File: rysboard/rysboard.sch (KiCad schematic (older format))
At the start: 9 parts, among them J1 RPi4, J17 Conn_01x03, J18 Conn_01x05, U4 STM32G031K8Ux

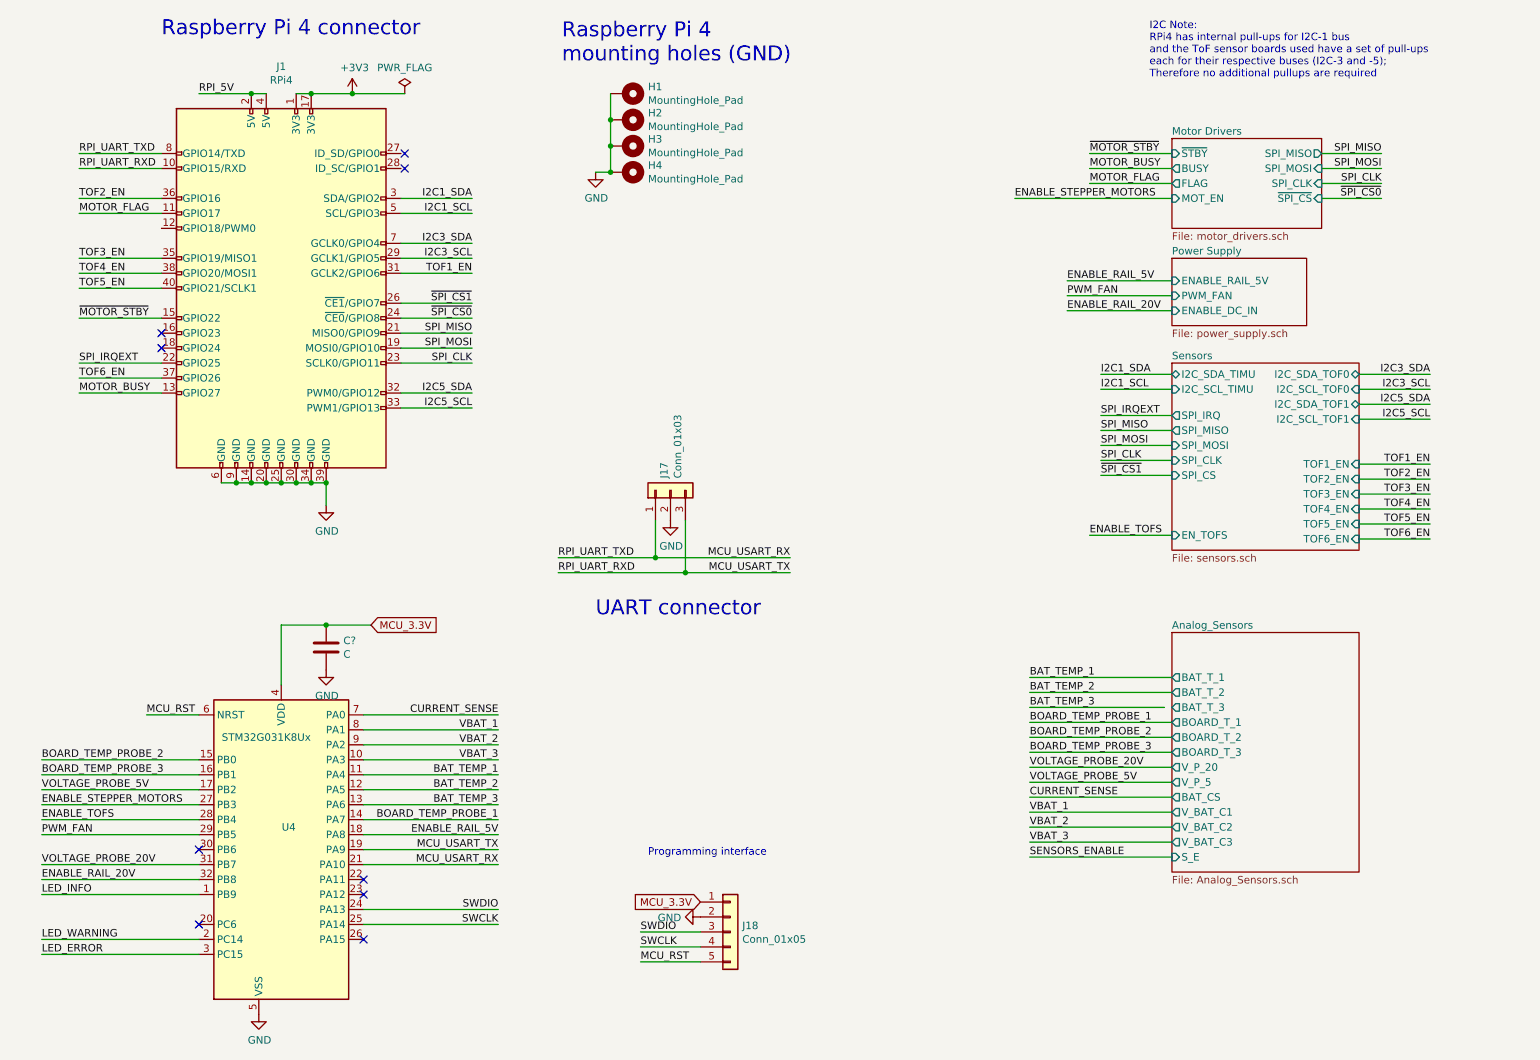
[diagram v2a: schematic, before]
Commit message: new mosfet footprints
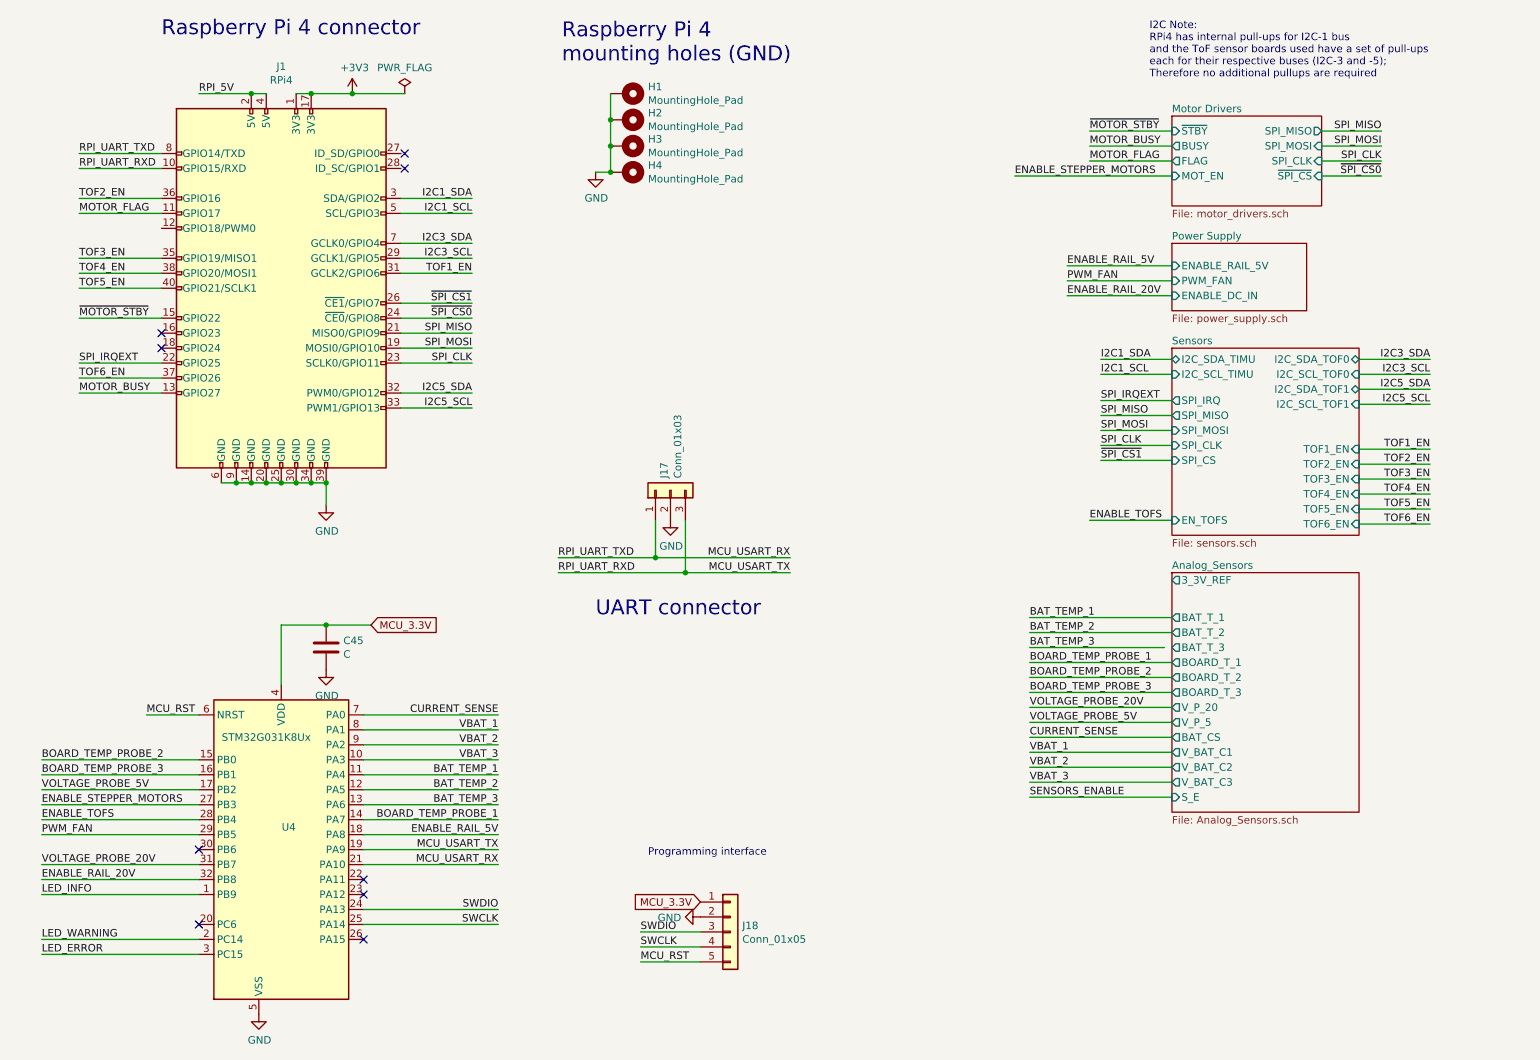
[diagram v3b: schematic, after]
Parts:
- gave numbers to parts that had none: 1
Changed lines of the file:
@@
 Raspberry Pi 4 connector
 $Sheet
-S 8250 2300 900  450
+S 8250 2200 900  450
 U 5E8FCBC6
 F0 "Power Supply" 50
 F1 "power_supply.sch" 50
-F2 "ENABLE_RAIL_5V" I L 8250 2450 50
-F3 "PWM_FAN" I L 8250 2550 50
-F4 "ENABLE_DC_IN" I L 8250 2650 50
+F2 "ENABLE_RAIL_5V" I L 8250 2350 50
+F3 "PWM_FAN" I L 8250 2450 50
+F4 "ENABLE_DC_IN" I L 8250 2550 50
 $EndSheet
 Text Label 3575 2700 2    50   ~ 0
@@
 Text Label 950  3200 0    50   ~ 0
 MOTOR_BUSY
-Text Label 7700 1800 0    50   ~ 0
+Text Label 7700 1650 0    50   ~ 0
 MOTOR_FLAG
-Text Label 7700 1600 0    50   ~ 0
+Text Label 7700 1450 0    50   ~ 0
 ~MOTOR_STBY
-Text Label 7700 1700 0    50   ~ 0
+Text Label 7700 1550 0    50   ~ 0
 MOTOR_BUSY
-Text Label 9650 1600 2    50   ~ 0
+Text Label 9650 1450 2    50   ~ 0
 SPI_MISO
-Text Label 9650 1700 2    50   ~ 0
+Text Label 9650 1550 2    50   ~ 0
 SPI_MOSI
-Text Label 9650 1800 2    50   ~ 0
+Text Label 9650 1650 2    50   ~ 0
 SPI_CLK
-Text Label 9650 1900 2    50   ~ 0
+Text Label 9650 1750 2    50   ~ 0
 ~SPI_CS0
+Text Label 7775 3350 0    50   ~ 0
+SPI_MISO
 Text Label 7775 3450 0    50   ~ 0
-SPI_MISO
+SPI_MOSI
 Text Label 7775 3550 0    50   ~ 0
-SPI_MOSI
+SPI_CLK
 Text Label 7775 3650 0    50   ~ 0
-SPI_CLK
-Text Label 7775 3750 0    50   ~ 0
 ~SPI_CS1
 Wire Wire Line
-	8250 3450 7775 3450
-Wire Wire Line
-	7775 3550 8250 3550
-Wire Wire Line
-	8250 3650 7775 3650
-Wire Wire Line
-	7775 3750 8250 3750
+	8250 3350 7775 3350
+Wire Wire Line
+	7775 3450 8250 3450
+Wire Wire Line
+	8250 3550 7775 3550
+Wire Wire Line
+	7775 3650 8250 3650
+Wire Wire Line
+	9500 3575 9975 3575
 Wire Wire Line
 	9500 3675 9975 3675
+Text Label 9975 3575 2    50   ~ 0
+TOF1_EN
+Text Label 9975 3675 2    50   ~ 0
+TOF2_EN
+Text Label 7775 3250 0    50   ~ 0
+SPI_IRQEXT
 Wire Wire Line
 	9500 3775 9975 3775
-Text Label 9975 3675 2    50   ~ 0
-TOF1_EN
 Text Label 9975 3775 2    50   ~ 0
-TOF2_EN
-Text Label 7775 3350 0    50   ~ 0
-SPI_IRQEXT
+TOF3_EN
+Text Label 9975 3875 2    50   ~ 0
+TOF4_EN
+Text Label 9975 3975 2    50   ~ 0
+TOF5_EN
+Text Label 9975 4075 2    50   ~ 0
+TOF6_EN
 Wire Wire Line
 	9500 3875 9975 3875
-Text Label 9975 3875 2    50   ~ 0
-TOF3_EN
-Text Label 9975 3975 2    50   ~ 0
-TOF4_EN
-Text Label 9975 4075 2    50   ~ 0
-TOF5_EN
-Text Label 9975 4175 2    50   ~ 0
-TOF6_EN
 Wire Wire Line
 	9500 3975 9975 3975
 Wire Wire Line
 	9500 4075 9975 4075
-Wire Wire Line
-	9500 4175 9975 4175
 NoConn ~ 3125 1700
 NoConn ~ 3125 1600
@@
 I2C5_SCL
 Wire Wire Line
-	7775 3350 8250 3350
+	7775 3250 8250 3250
 $Sheet
-S 8250 3000 1250 1250
+S 8250 2900 1250 1250
 U 5EA6D11C
 F0 "Sensors" 50
 F1 "sensors.sch" 50
-F2 "TOF6_EN" I R 9500 4175 50
-F3 "TOF5_EN" I R 9500 4075 50
-F4 "TOF4_EN" I R 9500 3975 50
-F5 "TOF2_EN" I R 9500 3775 50
-F6 "TOF1_EN" I R 9500 3675 50
-F7 "TOF3_EN" I R 9500 3875 50
-F8 "SPI_MOSI" I L 8250 3550 50
-F9 "SPI_MISO" O L 8250 3450 50
-F10 "SPI_CLK" I L 8250 3650 50
-F11 "SPI_CS" I L 8250 3750 50
-F12 "SPI_IRQ" O L 8250 3350 50
-F13 "I2C_SCL_TOF0" I R 9500 3175 50
-F14 "I2C_SDA_TOF0" B R 9500 3075 50
-F15 "I2C_SCL_TIMU" I L 8250 3175 50
-F16 "I2C_SDA_TIMU" B L 8250 3075 50
-F17 "I2C_SCL_TOF1" I R 9500 3375 50
-F18 "I2C_SDA_TOF1" B R 9500 3275 50
-F19 "EN_TOFS" I L 8250 4150 50
+F2 "TOF6_EN" I R 9500 4075 50
+F3 "TOF5_EN" I R 9500 3975 50
+F4 "TOF4_EN" I R 9500 3875 50
+F5 "TOF2_EN" I R 9500 3675 50
+F6 "TOF1_EN" I R 9500 3575 50
+F7 "TOF3_EN" I R 9500 3775 50
+F8 "SPI_MOSI" I L 8250 3450 50
+F9 "SPI_MISO" O L 8250 3350 50
+F10 "SPI_CLK" I L 8250 3550 50
+F11 "SPI_CS" I L 8250 3650 50
+F12 "SPI_IRQ" O L 8250 3250 50
+F13 "I2C_SCL_TOF0" I R 9500 3075 50
+F14 "I2C_SDA_TOF0" B R 9500 2975 50
+F15 "I2C_SCL_TIMU" I L 8250 3075 50
+F16 "I2C_SDA_TIMU" B L 8250 2975 50
+F17 "I2C_SCL_TOF1" I R 9500 3275 50
+F18 "I2C_SDA_TOF1" B R 9500 3175 50
+F19 "EN_TOFS" I L 8250 4050 50
 $EndSheet
 $Comp
@@
 RPI_UART_RXD
 Wire Wire Line
+	9500 2975 9975 2975
+Wire Wire Line
 	9500 3075 9975 3075
 Wire Wire Line
+	9500 3275 9975 3275
+Wire Wire Line
 	9500 3175 9975 3175
 Wire Wire Line
-	9500 3375 9975 3375
-Wire Wire Line
-	9500 3275 9975 3275
+	7775 2975 8250 2975
 Wire Wire Line
 	7775 3075 8250 3075
-Wire Wire Line
-	7775 3175 8250 3175
+Text Label 7775 2975 0    50   ~ 0
+I2C1_SDA
 Text Label 7775 3075 0    50   ~ 0
-I2C1_SDA
-Text Label 7775 3175 0    50   ~ 0
 I2C1_SCL
+Text Label 9975 2975 2    50   ~ 0
+I2C3_SDA
 Text Label 9975 3075 2    50   ~ 0
-I2C3_SDA
+I2C3_SCL
 Text Label 9975 3175 2    50   ~ 0
-I2C3_SCL
+I2C5_SDA
 Text Label 9975 3275 2    50   ~ 0
-I2C5_SDA
-Text Label 9975 3375 2    50   ~ 0
 I2C5_SCL
 Text Label 3575 2400 2    50   ~ 0
@@
 	4150 4400 5000 4400
 Connection ~ 5000 4400
+Text Label 7550 2350 0    50   ~ 0
+ENABLE_RAIL_5V
 Text Label 7550 2450 0    50   ~ 0
-ENABLE_RAIL_5V
+PWM_FAN
 Text Label 7550 2550 0    50   ~ 0
-PWM_FAN
-Text Label 7550 2650 0    50   ~ 0
 ENABLE_RAIL_20V
 Wire Wire Line
+	7550 2350 8250 2350
+Wire Wire Line
 	7550 2450 8250 2450
 Wire Wire Line
 	7550 2550 8250 2550
-Wire Wire Line
-	7550 2650 8250 2650
-Text Label 7700 4150 0    50   ~ 0
+Text Label 7700 4050 0    50   ~ 0
 ENABLE_TOFS
 Wire Wire Line
-	7700 4150 8250 4150
+	7700 4050 8250 4050
 $Sheet
-S 8250 4800 1250 1600
+S 8250 4400 1250 1600
 U 60370950
 F0 "Analog_Sensors" 50
 F1 "Analog_Sensors.sch" 50
-F2 "BAT_T_1" O L 8250 5100 50
-F3 "BAT_T_2" O L 8250 5200 50
-F4 "BAT_T_3" O L 8250 5300 50
-F5 "BOARD_T_1" O L 8250 5400 50
-F6 "BOARD_T_2" O L 8250 5500 50
-F7 "BOARD_T_3" O L 8250 5600 50
-F8 "V_P_20" O L 8250 5700 50
-F9 "V_P_5" O L 8250 5800 50
-F10 "BAT_CS" O L 8250 5900 50
-F11 "V_BAT_C1" O L 8250 6000 50
-F12 "V_BAT_C2" O L 8250 6100 50
-F13 "V_BAT_C3" O L 8250 6200 50
-F14 "S_E" I L 8250 6300 50
+F2 "BAT_T_1" O L 8250 4700 50
+F3 "BAT_T_2" O L 8250 4800 50
+F4 "BAT_T_3" O L 8250 4900 50
+F5 "BOARD_T_1" O L 8250 5000 50
+F6 "BOARD_T_2" O L 8250 5100 50
+F7 "BOARD_T_3" O L 8250 5200 50
+F8 "V_P_20" O L 8250 5300 50
+F9 "V_P_5" O L 8250 5400 50
+F10 "BAT_CS" O L 8250 5500 50
+F11 "V_BAT_C1" O L 8250 5600 50
+F12 "V_BAT_C2" O L 8250 5700 50
+F13 "V_BAT_C3" O L 8250 5800 50
+F14 "S_E" I L 8250 5900 50
+F15 "3_3V_REF" O L 8250 4450 50
 $EndSheet
-Text Label 7300 5500 0    50   ~ 0
+Text Label 7300 5100 0    50   ~ 0
 BOARD_TEMP_PROBE_2
-Text Label 7300 5600 0    50   ~ 0
+Text Label 7300 5200 0    50   ~ 0
 BOARD_TEMP_PROBE_3
-Text Label 7300 5400 0    50   ~ 0
+Text Label 7300 5000 0    50   ~ 0
 BOARD_TEMP_PROBE_1
-Text Label 7300 5300 0    50   ~ 0
+Text Label 7300 4900 0    50   ~ 0
 BAT_TEMP_3
-Text Label 7300 5200 0    50   ~ 0
+Text Label 7300 4800 0    50   ~ 0
 BAT_TEMP_2
-Text Label 7300 5100 0    50   ~ 0
+Text Label 7300 4700 0    50   ~ 0
 BAT_TEMP_1
 Text Notes 4750 6300 0    50   ~ 0
 Programming interface\n
+Text Label 7300 5300 0    50   ~ 0
+VOLTAGE_PROBE_20V
+Wire Wire Line
+	700  6350 1750 6350
+Wire Wire Line
+	700  5850 1750 5850
+Text Label 7300 5400 0    50   ~ 0
+VOLTAGE_PROBE_5V
+Text Label 7300 5500 0    50   ~ 0
+CURRENT_SENSE
+Text Label 7300 5600 0    50   ~ 0
+VBAT_1
 Text Label 7300 5700 0    50   ~ 0
-VOLTAGE_PROBE_20V
-Wire Wire Line
-	700  6350 1750 6350
-Wire Wire Line
-	700  5850 1750 5850
+VBAT_2
 Text Label 7300 5800 0    50   ~ 0
-VOLTAGE_PROBE_5V
-Text Label 7300 5900 0    50   ~ 0
-CURRENT_SENSE
-Text Label 7300 6000 0    50   ~ 0
-VBAT_1
-Text Label 7300 6100 0    50   ~ 0
-VBAT_2
-Text Label 7300 6200 0    50   ~ 0
 VBAT_3
 Wire Wire Line
-	7300 6200 8250 6200
-Wire Wire Line
-	8250 6100 7300 6100
-Wire Wire Line
-	7300 6000 8250 6000
-Wire Wire Line
-	8250 5900 7300 5900
-Wire Wire Line
 	7300 5800 8250 5800
 Wire Wire Line
@@
 	7300 5400 8250 5400
 Wire Wire Line
-	8200 5300 7300 5300
+	8250 5300 7300 5300
 Wire Wire Line
 	7300 5200 8250 5200
 Wire Wire Line
 	8250 5100 7300 5100
+Wire Wire Line
+	7300 5000 8250 5000
+Wire Wire Line
+	8200 4900 7300 4900
+Wire Wire Line
+	7300 4800 8250 4800
+Wire Wire Line
+	8250 4700 7300 4700
 $Comp
 L rysboard:STM32G031K8Ux U4
@@
 NoConn ~ 1750 6750
 NoConn ~ 1750 6250
-Text Label 7200 1900 0    50   ~ 0
+Text Label 7200 1750 0    50   ~ 0
 ENABLE_STEPPER_MOTORS
 $Sheet
-S 8250 1500 1000 600
+S 8250 1350 1000 600
 U 5EB7428E
 F0 "Motor Drivers" 50
 F1 "motor_drivers.sch" 50
-F2 "~STBY" I L 8250 1600 50
-F3 "~SPI_CS" I R 9250 1900 50
-F4 "SPI_CLK" I R 9250 1800 50
-F5 "SPI_MISO" O R 9250 1600 50
-F6 "SPI_MOSI" I R 9250 1700 50
-F7 "BUSY" O L 8250 1700 50
-F8 "FLAG" O L 8250 1800 50
-F9 "MOT_EN" I L 8250 1900 50
+F2 "~STBY" I L 8250 1450 50
+F3 "~SPI_CS" I R 9250 1750 50
+F4 "SPI_CLK" I R 9250 1650 50
+F5 "SPI_MISO" O R 9250 1450 50
+F6 "SPI_MOSI" I R 9250 1550 50
+F7 "BUSY" O L 8250 1550 50
+F8 "FLAG" O L 8250 1650 50
+F9 "MOT_EN" I L 8250 1750 50
 $EndSheet
 Wire Wire Line
-	7700 1600 8250 1600
-Wire Wire Line
-	8250 1700 7700 1700
-Wire Wire Line
-	7700 1800 8250 1800
-Wire Wire Line
-	7200 1900 8250 1900
-Wire Wire Line
-	9250 1600 9650 1600
-Wire Wire Line
-	9650 1700 9250 1700
-Wire Wire Line
-	9650 1800 9250 1800
-Wire Wire Line
-	9650 1900 9250 1900
-Text Label 7300 6300 0    50   ~ 0
+	7700 1450 8250 1450
+Wire Wire Line
+	8250 1550 7700 1550
+Wire Wire Line
+	7700 1650 8250 1650
+Wire Wire Line
+	7200 1750 8250 1750
+Wire Wire Line
+	9250 1450 9650 1450
+Wire Wire Line
+	9650 1550 9250 1550
+Wire Wire Line
+	9650 1650 9250 1650
+Wire Wire Line
+	9650 1750 9250 1750
+Text Label 7300 5900 0    50   ~ 0
 SENSORS_ENABLE
 Wire Wire Line
-	7300 6300 8250 6300
-$Comp
-L Device:C C?
+	7300 5900 8250 5900
+$Comp
+L Device:C C45
 U 1 1 603CCD3F
 P 2600 4900
-F 0 "C?" H 2715 4946 50  0000 L CNN
+F 0 "C45" H 2715 4946 50  0000 L CNN
 F 1 "C" H 2715 4855 50  0000 L CNN
 F 2 "" H 2638 4750 50  0001 C CNN
@@
 	2600 4750 2300 4750
 $Comp
-L power:GND #PWR?
+L power:GND #PWR060
 U 1 1 603D4B7E
 P 2600 5050
-F 0 "#PWR?" H 2600 4800 50  0001 C CNN
+F 0 "#PWR060" H 2600 4800 50  0001 C CNN
 F 1 "GND" H 2605 4877 50  0000 C CNN
 F 2 "" H 2600 5050 50  0001 C CNN

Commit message: more work done
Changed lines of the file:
@@
 Raspberry Pi 4 connector
 $Sheet
-S 8250 2200 900  450
+S 8275 2200 900  525
 U 5E8FCBC6
 F0 "Power Supply" 50
 F1 "power_supply.sch" 50
-F2 "ENABLE_RAIL_5V" I L 8250 2350 50
-F3 "PWM_FAN" I L 8250 2450 50
-F4 "ENABLE_DC_IN" I L 8250 2550 50
+F2 "ENABLE_RAIL_5V" I L 8275 2350 50
+F3 "PWM_FAN" I L 8275 2450 50
+F4 "ENABLE_DC_IN" I L 8275 2550 50
+F5 "ENABLE_CHARGING" I L 8275 2650 50
 $EndSheet
 Text Label 3575 2700 2    50   ~ 0
@@
 ENABLE_RAIL_20V
 Wire Wire Line
-	7550 2350 8250 2350
-Wire Wire Line
-	7550 2450 8250 2450
-Wire Wire Line
-	7550 2550 8250 2550
+	7550 2350 8275 2350
+Wire Wire Line
+	7550 2450 8275 2450
+Wire Wire Line
+	7550 2550 8275 2550
 Text Label 7700 4050 0    50   ~ 0
 ENABLE_TOFS

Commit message: more footprints
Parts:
- C45: value C -> 0.1uF; footprint (none) -> Capacitor_SMD:C_0603_1608Metric
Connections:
- net BOARD_TEMP_PROBE_2 renamed CHASSIS_TEMP_PROBE_1
- net BOARD_TEMP_PROBE_3 renamed CHASSIS_TEMP_PROBE_2
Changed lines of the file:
@@
 Text Label 3750 6050 2    50   ~ 0
 BOARD_TEMP_PROBE_1
-Text Label 700  5650 0    50   ~ 0
-BOARD_TEMP_PROBE_2
-Text Label 700  5750 0    50   ~ 0
-BOARD_TEMP_PROBE_3
 Text Label 700  5850 0    50   ~ 0
 VOLTAGE_PROBE_5V
@@
 F4 "BAT_T_3" O L 8250 4900 50
 F5 "BOARD_T_1" O L 8250 5000 50
-F6 "BOARD_T_2" O L 8250 5100 50
-F7 "BOARD_T_3" O L 8250 5200 50
+F6 "CHASSIS_T_1" O L 8250 5100 50
+F7 "CHASSIS_T_2" O L 8250 5200 50
 F8 "V_P_20" O L 8250 5300 50
 F9 "V_P_5" O L 8250 5400 50
@@
 $EndSheet
 Text Label 7300 5100 0    50   ~ 0
-BOARD_TEMP_PROBE_2
+CHASSIS_TEMP_PROBE_1
 Text Label 7300 5200 0    50   ~ 0
-BOARD_TEMP_PROBE_3
+CHASSIS_TEMP_PROBE_2
 Text Label 7300 5000 0    50   ~ 0
 BOARD_TEMP_PROBE_1
@@
 P 2600 4900
 F 0 "C45" H 2715 4946 50  0000 L CNN
-F 1 "C" H 2715 4855 50  0000 L CNN
-F 2 "" H 2638 4750 50  0001 C CNN
+F 1 "0.1uF" H 2715 4855 50  0000 L CNN
+F 2 "Capacitor_SMD:C_0603_1608Metric" H 2638 4750 50  0001 C CNN
 F 3 "~" H 2600 4900 50  0001 C CNN
 	1    2600 4900
@@
 	1    0    0    -1
 $EndComp
+Text Label 700  5650 0    50   ~ 0
+CHASSIS_TEMP_PROBE_1
+Text Label 700  5750 0    50   ~ 0
+CHASSIS_TEMP_PROBE_2
 $EndSCHEMATC
